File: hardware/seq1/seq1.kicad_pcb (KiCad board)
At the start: 2 copper layers, 132 x 80 mm, 43 parts, among them J4 Conn_02x08_Odd_Even, SW1 SW_Push, SW10 SW_Push, SW11 SW_Push, SW2 SW_Push, SW3 SW_Push, SW4 SW_Push, SW5 SW_Push, SW6 SW_Push, SW7 SW_Push, SW8 SW_Push, SW9 PEC12R-3220F-S0024, U1 74HCT1G125GW, U2 74HC4051, U3 74HC4051, U4 Adafruit QTPy SAMD21, U5 128x64 0.96" OLED I2C

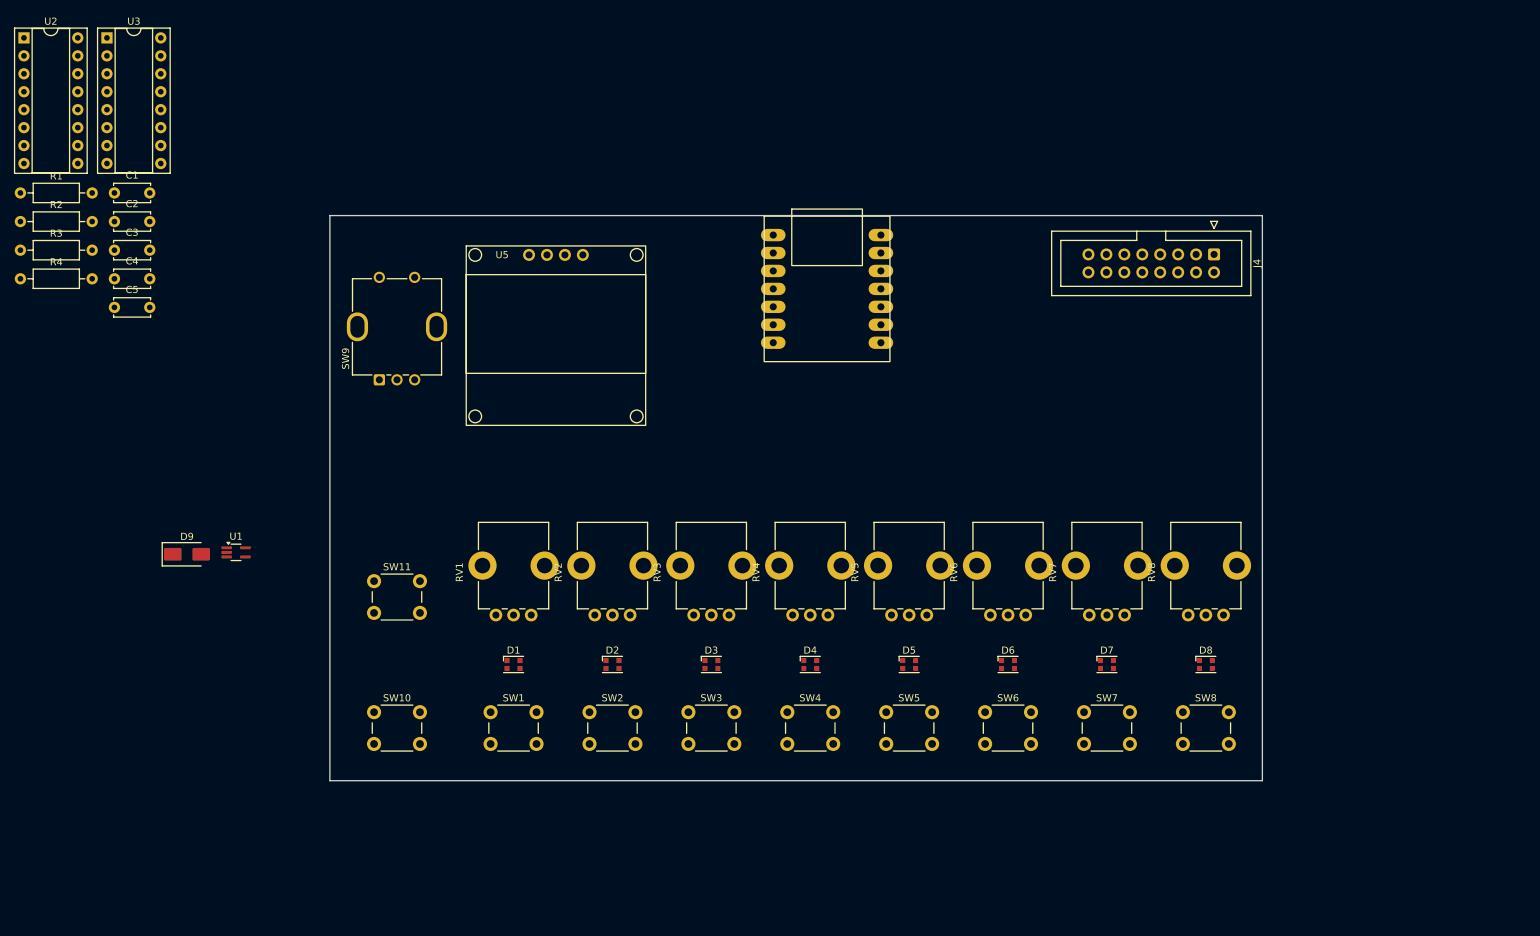
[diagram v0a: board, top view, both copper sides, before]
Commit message: menu system and adjustment through the physical interface
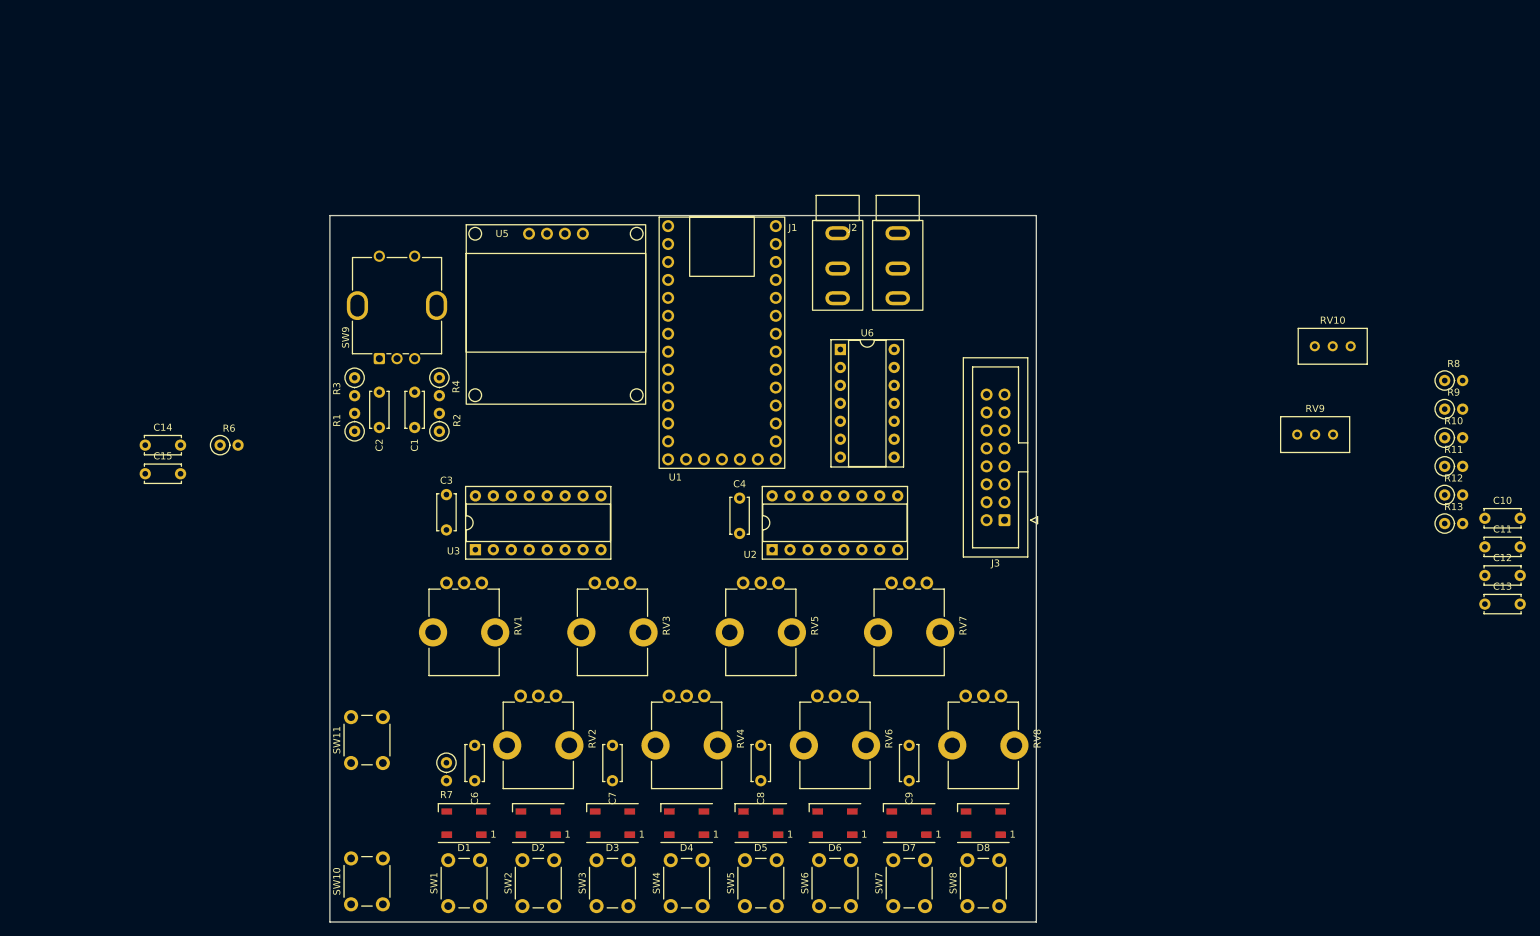
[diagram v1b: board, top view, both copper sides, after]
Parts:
- removed C5: 1u, Capacitor_THT:C_Disc_D5.0mm_W2.5mm_P5.00mm
- removed D9: SS16, Diode_SMD:D_SMA
- removed J4: Conn_02x08_Odd_Even, Connector_IDC:IDC-Header_2x08_P2.54mm_Vertical
- removed U4: Adafruit QTPy SAMD21, Module_Custom:Adafruit_QtPY_SAMD21
- added C10: 1u, Capacitor_THT:C_Disc_D5.0mm_W2.5mm_P5.00mm, F.Cu at (243.5, 62.9)
- added C11: 1u, Capacitor_THT:C_Disc_D5.0mm_W2.5mm_P5.00mm, F.Cu at (243.5, 66.9)
- added C12: 100p, Capacitor_THT:C_Disc_D5.0mm_W2.5mm_P5.00mm, F.Cu at (243.5, 71.0)
- added C13: 100p, Capacitor_THT:C_Disc_D5.0mm_W2.5mm_P5.00mm, F.Cu at (243.5, 75.0)
- added C14: 10n, Capacitor_THT:C_Disc_D5.0mm_W2.5mm_P5.00mm, F.Cu at (53.9, 52.5)
- added C15: 10n, Capacitor_THT:C_Disc_D5.0mm_W2.5mm_P5.00mm, F.Cu at (53.9, 56.5)
- added C6: 1u, Capacitor_THT:C_Disc_D5.0mm_W2.5mm_P5.00mm, F.Cu at (100.5, 100.0)
- added C7: 1u, Capacitor_THT:C_Disc_D5.0mm_W2.5mm_P5.00mm, F.Cu at (120.0, 100.0)
- added C8: 1u, Capacitor_THT:C_Disc_D5.0mm_W2.5mm_P5.00mm, F.Cu at (141.0, 100.0)
- added C9: 1u, Capacitor_THT:C_Disc_D5.0mm_W2.5mm_P5.00mm, F.Cu at (162.0, 100.0)
- added J1: AudioJack2_SwitchT, Connector_Audio_Custom:Mono_Jack_3.5mm_THT_Horizontal, F.Cu at (151.9, 27.1)
- added J2: AudioJack2_SwitchT, Connector_Audio_Custom:Mono_Jack_3.5mm_THT_Horizontal, F.Cu at (160.4, 27.1)
- added J3: Conn_02x08_Odd_Even, Connector_IDC:IDC-Header_2x08_P2.54mm_Vertical, F.Cu at (175.5, 63.1)
- added R10: 10k, Resistor_THT:R_Axial_DIN0207_L6.3mm_D2.5mm_P2.54mm_Vertical, F.Cu at (237.8, 51.5)
- added R11: 10k, Resistor_THT:R_Axial_DIN0207_L6.3mm_D2.5mm_P2.54mm_Vertical, F.Cu at (237.8, 55.5)
- added R12: 20k, Resistor_THT:R_Axial_DIN0207_L6.3mm_D2.5mm_P2.54mm_Vertical, F.Cu at (237.8, 59.5)
- added R13: 20k, Resistor_THT:R_Axial_DIN0207_L6.3mm_D2.5mm_P2.54mm_Vertical, F.Cu at (237.8, 63.6)
- added R6: 10k, Resistor_THT:R_Axial_DIN0207_L6.3mm_D2.5mm_P2.54mm_Vertical, F.Cu at (64.5, 52.5)
- added R7: 330, Resistor_THT:R_Axial_DIN0207_L6.3mm_D2.5mm_P2.54mm_Vertical, F.Cu at (96.5, 97.5)
- added R8: 10k, Resistor_THT:R_Axial_DIN0207_L6.3mm_D2.5mm_P2.54mm_Vertical, F.Cu at (237.8, 43.4)
- added R9: 10k, Resistor_THT:R_Axial_DIN0207_L6.3mm_D2.5mm_P2.54mm_Vertical, F.Cu at (237.8, 47.4)
- added RV10: 50k, Potentiometer_THT:Potentiometer_Bourns_3296W_Vertical, F.Cu at (224.5, 38.5)
- added RV9: 50k, Potentiometer_THT:Potentiometer_Bourns_3296W_Vertical, F.Cu at (222.0, 51.0)
- added U6: TL074, Package_DIP:DIP-14_W7.62mm_Socket, F.Cu at (152.3, 39.0)
- D1, D2, D3, D4, D5, D6, D7, D8: footprint LED_SMD:LED_WS2812B-2020_PLCC4_2.0x2.0mm -> LED_SMD:LED_WS2812B_PLCC4_5.0x5.0mm_P3.2mm
- R1, R2, R3, R4: footprint Resistor_THT:R_Axial_DIN0207_L6.3mm_D2.5mm_P10.16mm_Horizontal -> Resistor_THT:R_Axial_DIN0207_L6.3mm_D2.5mm_P2.54mm_Vertical
- U1: value 74HCT1G125GW -> ~; footprint Package_TO_SOT_SMD:SOT-353_SC-70-5_Handsoldering -> Module_Custom:Adafruit_ItsyBitsy_M0_Express
- moved U2 128.3 mm to (142.6, 67.3), turned to 90 degrees
- moved C4 93.8 mm to (138.0, 60.0), turned to -90 degrees
- moved U3 89.3 mm to (100.6, 67.3), turned to 90 degrees
- moved U1 74.9 mm to (135.5, 38.0)
- moved R2 66.3 mm to (95.5, 50.5), turned to 90 degrees
- moved R4 60.9 mm to (95.5, 43.0), turned to -90 degrees
- moved C3 58.4 mm to (96.5, 59.5), turned to -90 degrees
- moved R1 58.1 mm to (83.5, 50.5), turned to 90 degrees
- moved C1 51.0 mm to (92.0, 45.0), turned to -90 degrees
- moved R3 50.6 mm to (83.5, 43.0), turned to -90 degrees
- moved C2 44.6 mm to (87.0, 45.0), turned to -90 degrees
- moved SW8 41.0 mm to (170.2, 117.8), turned to 90 degrees
- moved D8 38.7 mm to (172.5, 106.0), turned to 180 degrees
- moved SW7 38.5 mm to (159.8, 117.8), turned to 90 degrees
- moved RV8 38.3 mm to (170.0, 88.0), turned to -90 degrees
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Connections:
- net /ADR0 renamed /muxdinputs/MUX_ADDR0
- net /ADR1 renamed /muxdinputs/MUX_ADDR1
- net /ADR2 renamed /muxdinputs/MUX_ADDR2
- net /SW_MUX renamed /muxdinputs/SW_MUX
- D1 pad 4: /NPXL_D5V -> Net-(D1-DIN)
- R1 pad 1: +3V3 -> /mcu/RSWA
- R1 pad 2: Net-(C2-Pad1) -> Net-(C1-Pad1)
- R2 pad 1: +3V3 -> /mcu/RSWB
- R2 pad 2: Net-(C1-Pad1) -> Net-(C2-Pad1)
- R3 pad 1: Net-(U4-D9/A9/MISO/PA09) -> +3V3
- R4 pad 1: Net-(U4-D8/A8/SCK/PA11) -> +3V3
- RV1 pad 2: Net-(U3-A0) -> Net-(U3-A4)
- RV2 pad 2: Net-(U3-A1) -> Net-(U3-A5)
- RV3 pad 2: Net-(U3-A3) -> Net-(U3-A7)
- RV4 pad 2: Net-(U3-A2) -> Net-(U3-A6)
- RV5 pad 2: Net-(U3-A6) -> Net-(U3-A2)
- RV6 pad 2: Net-(U3-A7) -> Net-(U3-A3)
- RV7 pad 2: Net-(U3-A5) -> Net-(U3-A1)
- RV8 pad 2: Net-(U3-A4) -> Net-(U3-A0)
- SW10 pad 2: /N_RUN -> /mcu/N_RUN
- SW11 pad 2: /N_MODE -> /mcu/N_MODE
- SW9 pad A: Net-(C2-Pad1) -> Net-(C1-Pad1)
- SW9 pad B: Net-(C1-Pad1) -> Net-(C2-Pad1)
- SW9 pad S1: /ROT_SW -> GND
- SW9 pad S2: GND -> /mcu/ROT_SW
- U1 pad 1: GND -> unconnected-(U1-RST-Pad1)
- U1 pad 2: /NPXL_D -> +3V3
- U1 pad 3: GND -> +3V3_A
- U1 pad 4: /NPXL_D5V -> +5V
- U1 pad 5: +5V -> /mcu/CV
- U3 pad 3: /POT_MUX -> /muxdinputs/POT_MUX
- U5 pad 3: Net-(U4-D5/SCL/PA17) -> Net-(U1-D27/SCL/PA23)
- U5 pad 4: Net-(U4-D4/SDA/PA16) -> Net-(U1-D26/SDA/PA22)
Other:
- board size 132 x 80 mm -> 100 x 100 mm

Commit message: schematic and layout for v1 board
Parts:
- added C16: 47u, Capacitor_THT:CP_Radial_D5.0mm_P2.50mm, F.Cu at (116.6, 32.3)
- added C17: 1u, Capacitor_THT:C_Disc_D5.0mm_W2.5mm_P5.00mm, F.Cu at (165.7, 22.7)
- added C5: 220p, Capacitor_THT:C_Disc_D5.0mm_W2.5mm_P5.00mm, F.Cu at (117.5, 55.1)
- added D10: SB160, Diode_THT:D_DO-41_SOD81_P10.16mm_Horizontal, F.Cu at (104.4, 32.5)
- added D9: SB160, Diode_THT:D_DO-41_SOD81_P2.54mm_Vertical_AnodeUp, F.Cu at (101.6, 36.1)
- added J4: AudioJack2_SwitchT, Connector_Audio_Custom:Mono_Jack_3.5mm_THT_Horizontal, F.Cu at (86.4, 57.8)
- added J5: AudioJack2_SwitchT, Connector_Audio_Custom:Mono_Jack_3.5mm_THT_Horizontal, F.Cu at (86.4, 68.8)
- added J6: Conn_02x06_Odd_Even, Connector_PinHeader_2.54mm:PinHeader_2x06_P2.54mm_Vertical, F.Cu at (127.2, 29.2)
- added Q1: 2N3904, Package_TO_SOT_THT:TO-92_Inline, F.Cu at (107.6, 70.1)
- added R14: 10k, Resistor_THT:R_Axial_DIN0207_L6.3mm_D2.5mm_P2.54mm_Vertical, F.Cu at (112.5, 57.6)
- added R15: 10k, Resistor_THT:R_Axial_DIN0207_L6.3mm_D2.5mm_P2.54mm_Vertical, F.Cu at (112.5, 60.2)
- added R16: 1k, Resistor_THT:R_Axial_DIN0207_L6.3mm_D2.5mm_P2.54mm_Vertical, F.Cu at (106.7, 63.7)
- added R17: 100k, Resistor_THT:R_Axial_DIN0207_L6.3mm_D2.5mm_P2.54mm_Vertical, F.Cu at (97.1, 70.9)
- added R18: 10k, Resistor_THT:R_Axial_DIN0207_L6.3mm_D2.5mm_P2.54mm_Vertical, F.Cu at (112.0, 72.4)
- added R19: 4.7k, Resistor_THT:R_Axial_DIN0207_L6.3mm_D2.5mm_P10.16mm_Horizontal, F.Cu at (148.0, 57.3)
- added R20: 4.7k, Resistor_THT:R_Axial_DIN0207_L6.3mm_D2.5mm_P10.16mm_Horizontal, F.Cu at (144.8, 57.3)
- added R5: 1k, Resistor_THT:R_Axial_DIN0207_L6.3mm_D2.5mm_P10.16mm_Horizontal, F.Cu at (106.9, 41.6)
- added RV11: 50k, Potentiometer_THT:Potentiometer_Bourns_3296W_Vertical, F.Cu at (115.8, 64.7)
- added U7: TLV1117-33, Package_TO_SOT_SMD:SOT-223-3_TabPin2, F.Cu at (114.0, 26.7)
- C12, C13: value 100p -> 220p
- C15: value 10n -> 100n
- R12, R13: value 20k -> 10k
- R8: value 10k -> 1k
- R9: value 10k -> 0
- moved C13 149.3 mm to (95.0, 60.1), turned to 90 degrees
- moved C10 145.8 mm to (98.0, 52.6), turned to -90 degrees
- moved R8 144.5 mm to (95.0, 65.3), turned to 90 degrees
- moved R13 143.2 mm to (95.0, 52.6), turned to 90 degrees
- moved R10 142.9 mm to (95.0, 47.5), turned to 90 degrees
- moved R11 140.0 mm to (98.0, 62.7), turned to 90 degrees
- moved R9 139.8 mm to (98.0, 44.9), turned to -90 degrees
- moved C12 127.7 mm to (117.5, 50.0), turned to 180 degrees
- moved C11 126.8 mm to (117.5, 52.5), turned to 180 degrees
- moved R12 125.9 mm to (112.5, 47.5)
- moved RV10 124.8 mm to (102.4, 64.2), turned to 90 degrees
- moved RV9 106.0 mm to (116.6, 40.4)
- moved R3 93.4 mm to (176.9, 42.6)
- moved R1 93.4 mm to (176.9, 50.2)
- moved C2 86.4 mm to (173.4, 44.6)
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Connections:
- C12 pad 2: Net-(U6A-+) -> Net-(U6D-+)
- J1 pad T: Net-(J1-PadT) -> CV_O
- J2 pad T: Net-(J2-PadT) -> GATE_O
- J3 pad 1: -12V -> Net-(D9-K)
- J3 pad 10: +12V -> Net-(D10-A)
- J3 pad 13: /pwr/CV -> CV_O
- J3 pad 14: /pwr/CV -> CV_O
- J3 pad 15: /pwr/GATE -> GATE_O
- J3 pad 16: /pwr/GATE -> GATE_O
- J3 pad 2: -12V -> Net-(D9-K)
- J3 pad 9: +12V -> Net-(D10-A)
- R1 pad 1: /mcu/RSWA -> +3V3
- R1 pad 2: Net-(C1-Pad1) -> Net-(C2-Pad1)
- R10 pad 1: Net-(U6D-+) -> Net-(U6A-+)
- R12 pad 1: Net-(U6A-+) -> Net-(U6D-+)
- R12 pad 2: /outputs/CV -> CV
- R13 pad 2: /outputs/GATE -> SYNC_OUT
- R2 pad 1: /mcu/RSWB -> +3V3
- R2 pad 2: Net-(C2-Pad1) -> Net-(C1-Pad1)
- R3 pad 1: +3V3 -> /mcu/RSWA
- R4 pad 1: +3V3 -> /mcu/RSWB
- R6 pad 1: Net-(R5-Pad2) -> Net-(R5-Pad1)
- R6 pad 2: Net-(U6A--) -> Net-(U6D--)
- R7 pad 1: /neopxls/NPXL_D5V -> NPXL_D5V
- R8 pad 1: Net-(U6C-+) -> Net-(R11-Pad1)
- R8 pad 2: GND -> SYNC_OUT_O
- R9 pad 1: Net-(U6C-+) -> Net-(R9-Pad1)
- R9 pad 2: GND -> Net-(U6A--)
- RV9 pad 1: Net-(U6A--) -> Net-(U6D--)
- SW10 pad 2: /mcu/N_RUN -> /mcu/N_MODE
- SW11 pad 2: /mcu/N_MODE -> /mcu/N_RUN
- SW9 pad S1: GND -> /mcu/ROT_SW
- SW9 pad S2: /mcu/ROT_SW -> GND
- U1 pad 1: unconnected-(U1-RST-Pad1) -> /mcu/MCU_RST
- U1 pad 10: /mcu/ROT_SW -> SYNC_IN
- U1 pad 11: /mcu/RSWA -> SYNC_OUT
- U1 pad 12: /mcu/RSWB -> /mcu/N_MODE
- U1 pad 14: /mcu/N_MODE -> GATE
- U1 pad 18: unconnected-(U1-D3/A9/PA09-Pad18) -> /mcu/D3_A9
- U1 pad 19: unconnected-(U1-D4/A8/PA08-Pad19) -> /mcu/D4_A8
- U1 pad 20: unconnected-(U1-D0/A6/PA11-Pad20) -> MUX_ADDR0
- U1 pad 21: unconnected-(U1-D1/A7/PA10-Pad21) -> MUX_ADDR1
- U1 pad 24: /mcu/NPXL_D5V -> NPXL_D5V
- U1 pad 25: unconnected-(U1-D7/PA21-Pad25) -> MUX_ADDR2
- U1 pad 26: /mcu/SW_MUX -> SW_MUX
- U1 pad 27: /mcu/MUX_ADDR2 -> /mcu/RSWB
- U1 pad 28: /mcu/MUX_ADDR1 -> /mcu/RSWA
- U1 pad 29: /mcu/MUX_ADDR0 -> /mcu/ROT_SW
- U1 pad 30: /mcu/GATE -> /mcu/D13
- U1 pad 5: /mcu/CV -> CV
- U1 pad 6: unconnected-(U1-D15/A1/PB08-Pad6) -> /mcu/D15_A1
- U1 pad 7: unconnected-(U1-D16/A2/PB09-Pad7) -> /mcu/D16_A2
- U1 pad 8: unconnected-(U1-D17/A3/PA04-Pad8) -> /mcu/D17_A3
- U1 pad 9: /mcu/POT_MUX -> POT_MUX
- U2 pad 10: /muxdinputs/MUX_ADDR1 -> MUX_ADDR1
- U2 pad 11: /muxdinputs/MUX_ADDR0 -> MUX_ADDR0
- U2 pad 3: /muxdinputs/SW_MUX -> SW_MUX
- U2 pad 9: /muxdinputs/MUX_ADDR2 -> MUX_ADDR2
- U3 pad 10: /muxdinputs/MUX_ADDR1 -> MUX_ADDR1
- U3 pad 11: /muxdinputs/MUX_ADDR0 -> MUX_ADDR0
- U3 pad 3: /muxdinputs/POT_MUX -> POT_MUX
- U3 pad 9: /muxdinputs/MUX_ADDR2 -> MUX_ADDR2
- U6 pad 1: Net-(R5-Pad2) -> Net-(R9-Pad1)
- U6 pad 14: Net-(U6D--) -> Net-(R5-Pad1)
- U6 pad 8: Net-(U6C--) -> Net-(R15-Pad1)
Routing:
- net +3V3: track 0.00 -> 308.5 mm
- net +5V: track 0.00 -> 273.9 mm, vias 0 -> 8
- net Net-(U2-A0): track 0.00 -> 105.2 mm, vias 0 -> 1
- net Net-(U2-A1): track 0.00 -> 92.2 mm, vias 0 -> 1
- net /mcu/N_MODE: track 0.00 -> 86.5 mm
- net Net-(U2-A3): track 0.00 -> 82.0 mm, vias 0 -> 1
- net Net-(U2-A6): track 0.00 -> 76.0 mm, vias 0 -> 1
- net Net-(U2-A7): track 0.00 -> 74.2 mm, vias 0 -> 1
- net Net-(U2-A5): track 0.00 -> 73.3 mm, vias 0 -> 1
- net NPXL_D5V: track 0.00 -> 69.9 mm, vias 0 -> 1
- net Net-(U2-A2): track 0.00 -> 67.5 mm, vias 0 -> 1
- net Net-(U2-A4): track 0.00 -> 65.8 mm, vias 0 -> 1
- net /mcu/N_RUN: track 0.00 -> 62.0 mm
- net GATE_O: track 0.00 -> 56.6 mm
- net Net-(U3-A0): track 0.00 -> 52.5 mm, vias 0 -> 1
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- added copper zone on F.Cu, net +3V3_A
- added copper zone on B.Cu, net GND
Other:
- board text added: "3V3"
- board text added: "3V3A"
- board text added: "5V"
- board text added: "<CV"
- board text added: "<GATE"
- board text added: "<SYNC"
- board text added: ">SYNC"
- board text added: "A1"
- board text added: "A2"
- board text added: "A3"
- board text added: "D13"
- board text added: "D3"
- board text added: "D4"
- board text added: "GND"
- board text added: "MODE"
- board text added: "RST"

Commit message: layout clean up
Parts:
- added H1: MountingHole, MountingHole:MountingHole_3.5mm, F.Cu at (85.0, 81.0)
- added H2: MountingHole, MountingHole:MountingHole_3.5mm, F.Cu at (175.0, 81.0)
- added Ref**: Val**, Display_Custom:play_pause_6mm, F.Cu at (85.0, 106.5)
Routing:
- net +5V: track 273.9 -> 277.5 mm
- net Net-(U2-A6): track 76.0 -> 73.3 mm
- net Net-(U2-A4): track 65.8 -> 66.8 mm
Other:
- board text added: "JLCJLCJLCJLC"
- board text added: "SEQUENCER-1"
- board text added: "V1.0.20240414"
